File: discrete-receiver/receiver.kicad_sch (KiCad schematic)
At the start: 42 parts, among them J1 His Excellence, J3 Conn_01x04_Socket, J7 Her Excellency, T1 H1102NLT, T2 MABA-007159-000000, U16 PSA4-5043_, U18 SN74LVC1G3157DBVR, U19 SN74LVC1G3157DBVR, U2 OPA1612AxD, U20 SN74LVC1G3157DBVR, U3 OPA1612AxD, U5 ADE-12+

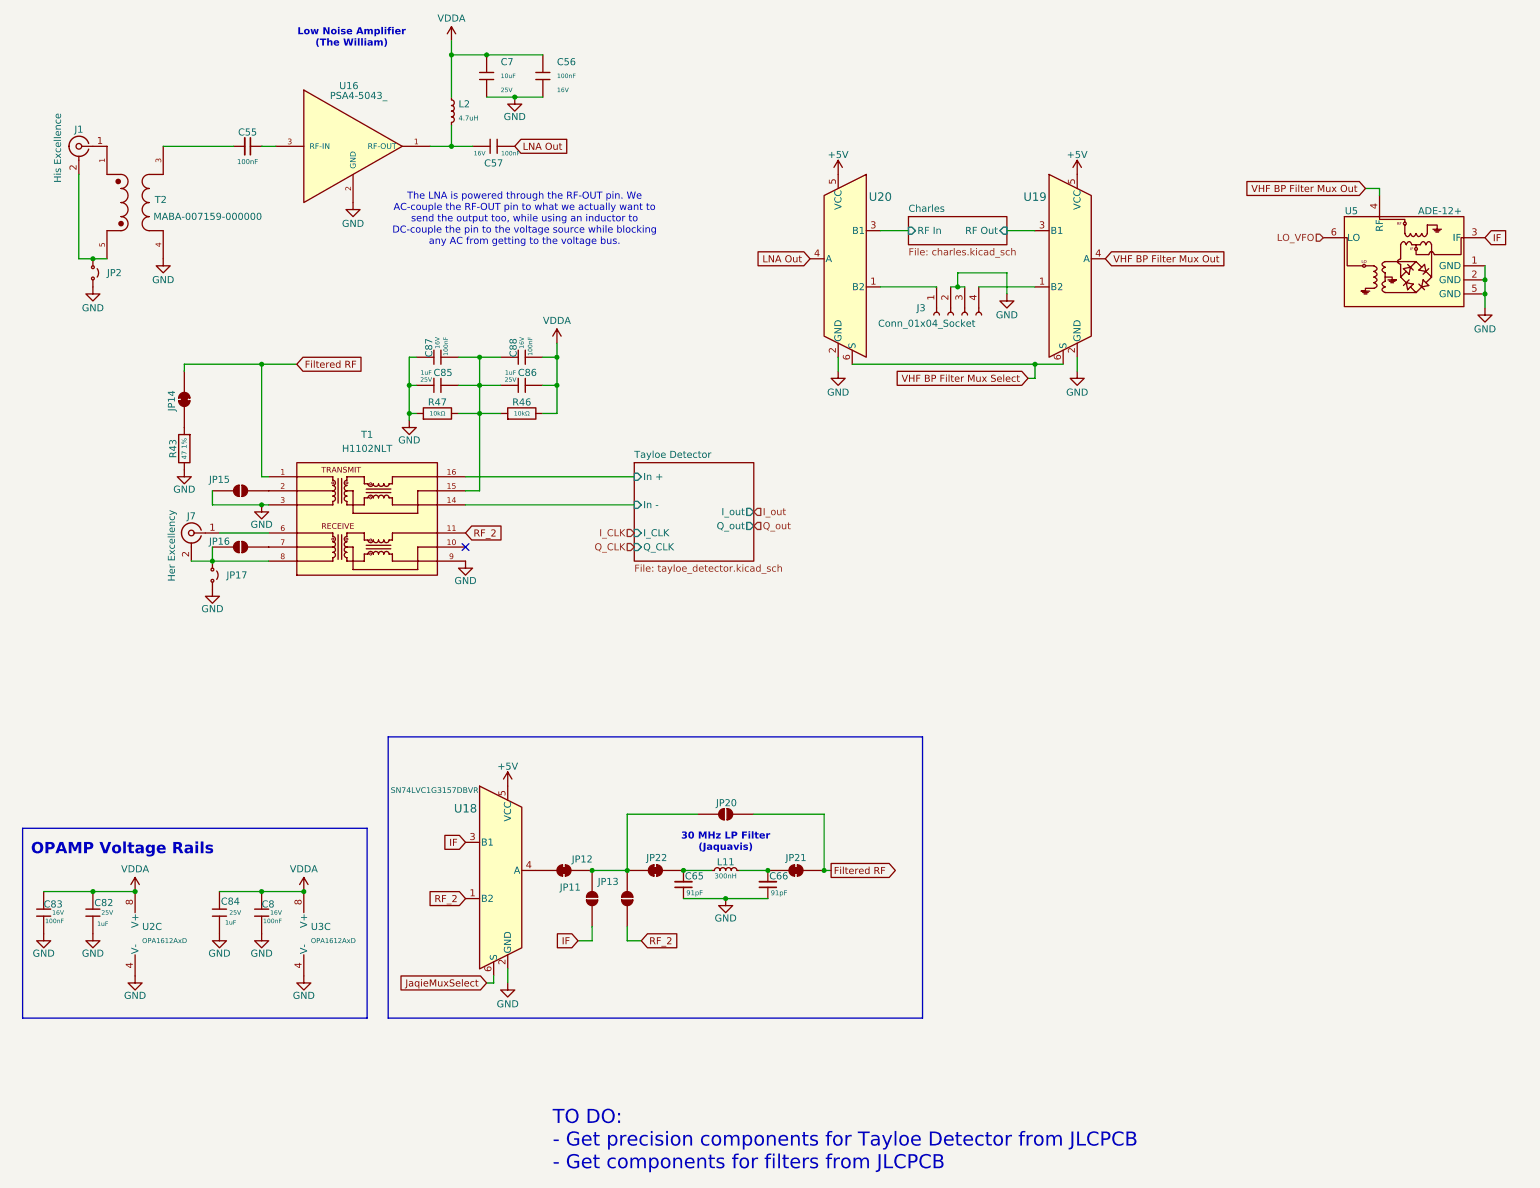
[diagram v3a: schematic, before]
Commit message: Subsheetified the receiver page
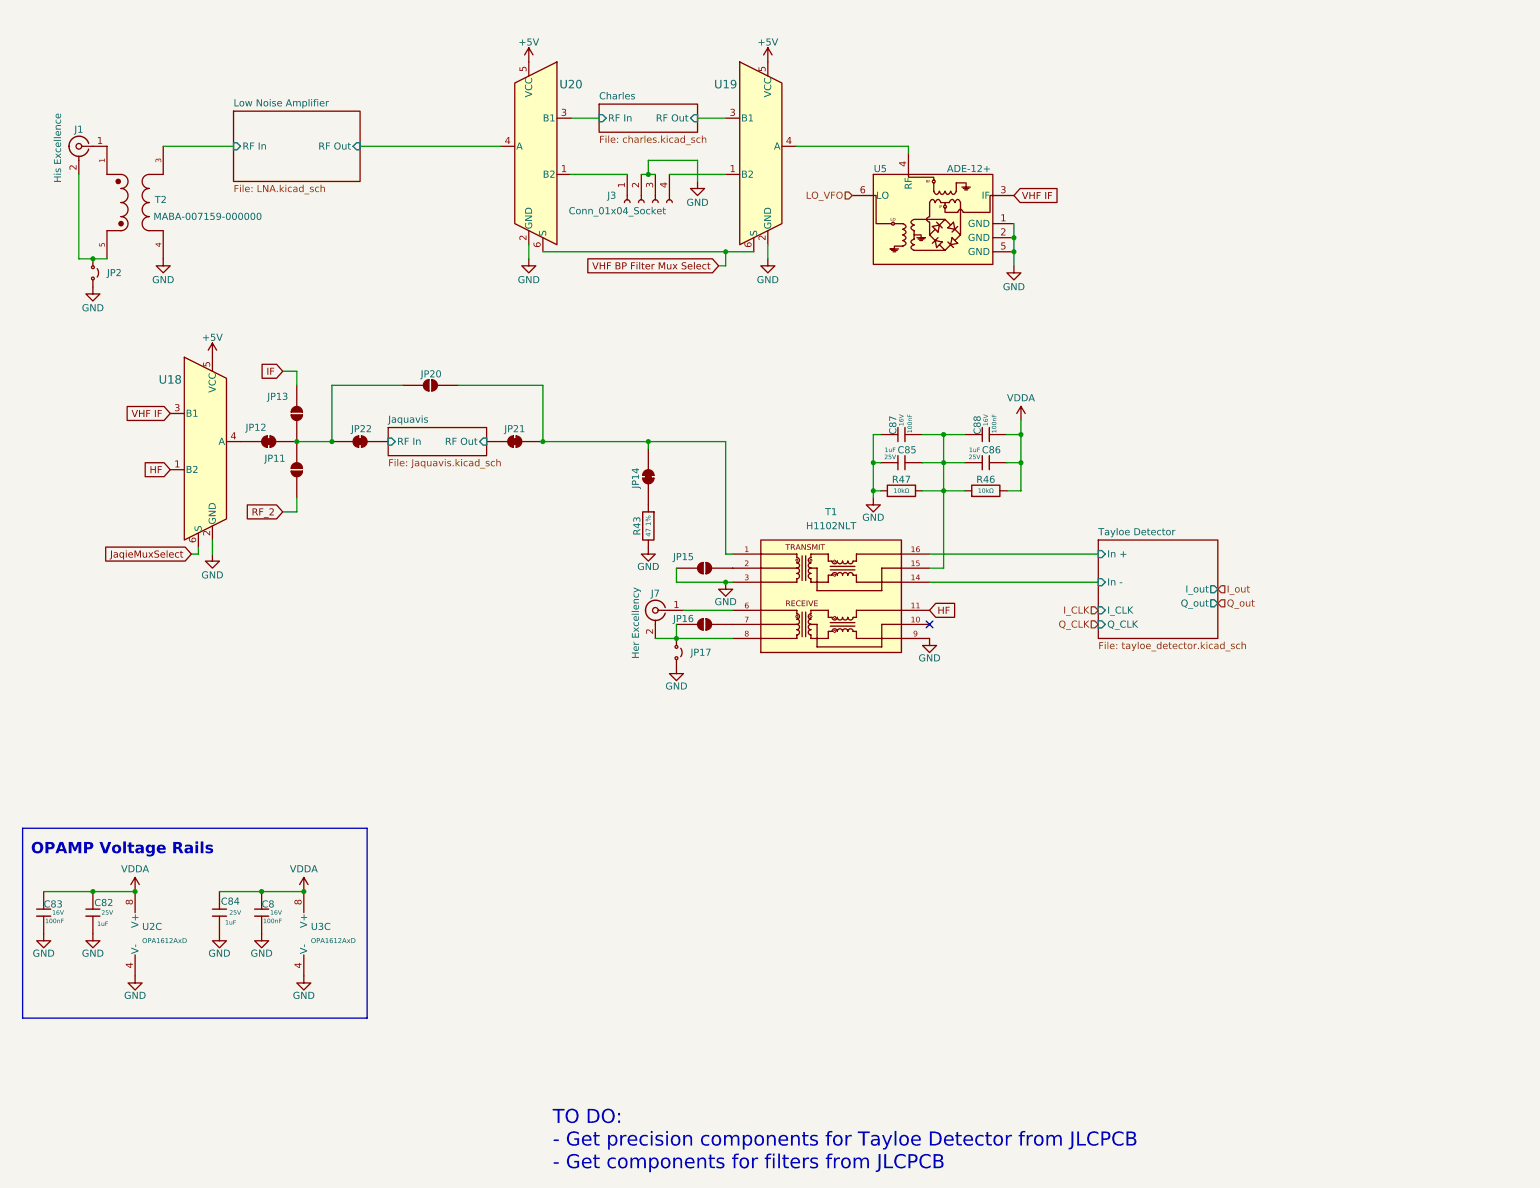
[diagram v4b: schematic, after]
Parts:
- removed C55: 100nF, symbol Device:C_Small
- removed C56, C57: 100nF, PCM_JLCPCB:C_0402, symbol PCM_JLCPCB-Capacitors:0402,100nF
- removed C65, C66: 91pF, symbol Device:C_Small
- removed C7: 10uF, PCM_JLCPCB:C_0603, symbol PCM_JLCPCB-Capacitors:0603,10uF,(2)
- removed L11: 300nH, symbol Device:L_Small
- removed L2: 4.7uH, symbol Device:L_Small
- removed U16: PSA4-5043_, PSA4-5043_:PSA4-5043_, symbol PSA4-5043_:PSA4-5043_
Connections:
- net IF: now also JP13.2 (B); no longer JP11.1 (A), U18.3 (B1), U5.3 (IF)
- net RF_2: now also JP11.1 (A); no longer JP13.1 (A), T1.11, U18.1 (B2)
- net at JP11.2 (B), JP12.2 (B), JP20.1 (A)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: now also JP13.1 (A); no longer JP13.2 (B)
- net Low Noise Amplifier/RF In: now reaches T2.3
- net Jaquavis/RF In: now reaches JP22.2 (B)
- net Jaquavis/RF Out: now reaches JP21.1 (A)
- net Filtered RF: no longer names the net of JP14.2 (B), JP20.2 (B), JP21.2 (B), T1.1
- net LNA Out renamed Low Noise Amplifier/RF Out
- net VHF BP Filter Mux Out: no longer names the net of U19.4 (A), U5.4 (RF)
- new net HF: T1.11, U18.1 (B2)
- new net VHF IF: U18.3 (B1), U5.3 (IF)
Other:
- added sheet Jaquavis (Jaquavis.kicad_sch)
- added sheet Low Noise Amplifier (LNA.kicad_sch)
- note removed: "30 MHz LP Filter (Jaquavis)"
- note removed: "Low Noise Amplifier (The William)"
- note removed: "The LNA is powered through the RF-OUT pin. We AC-couple the RF-OUT pin to what we actually want to send the output too, while using an inductor to DC-couple the pin to the voltage source while blocking any AC from getting to the voltage bus."
- moved on the sheet: C85, C86, C87, C88, J3, J7, JP14, JP15, JP16, JP17, R43, R46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

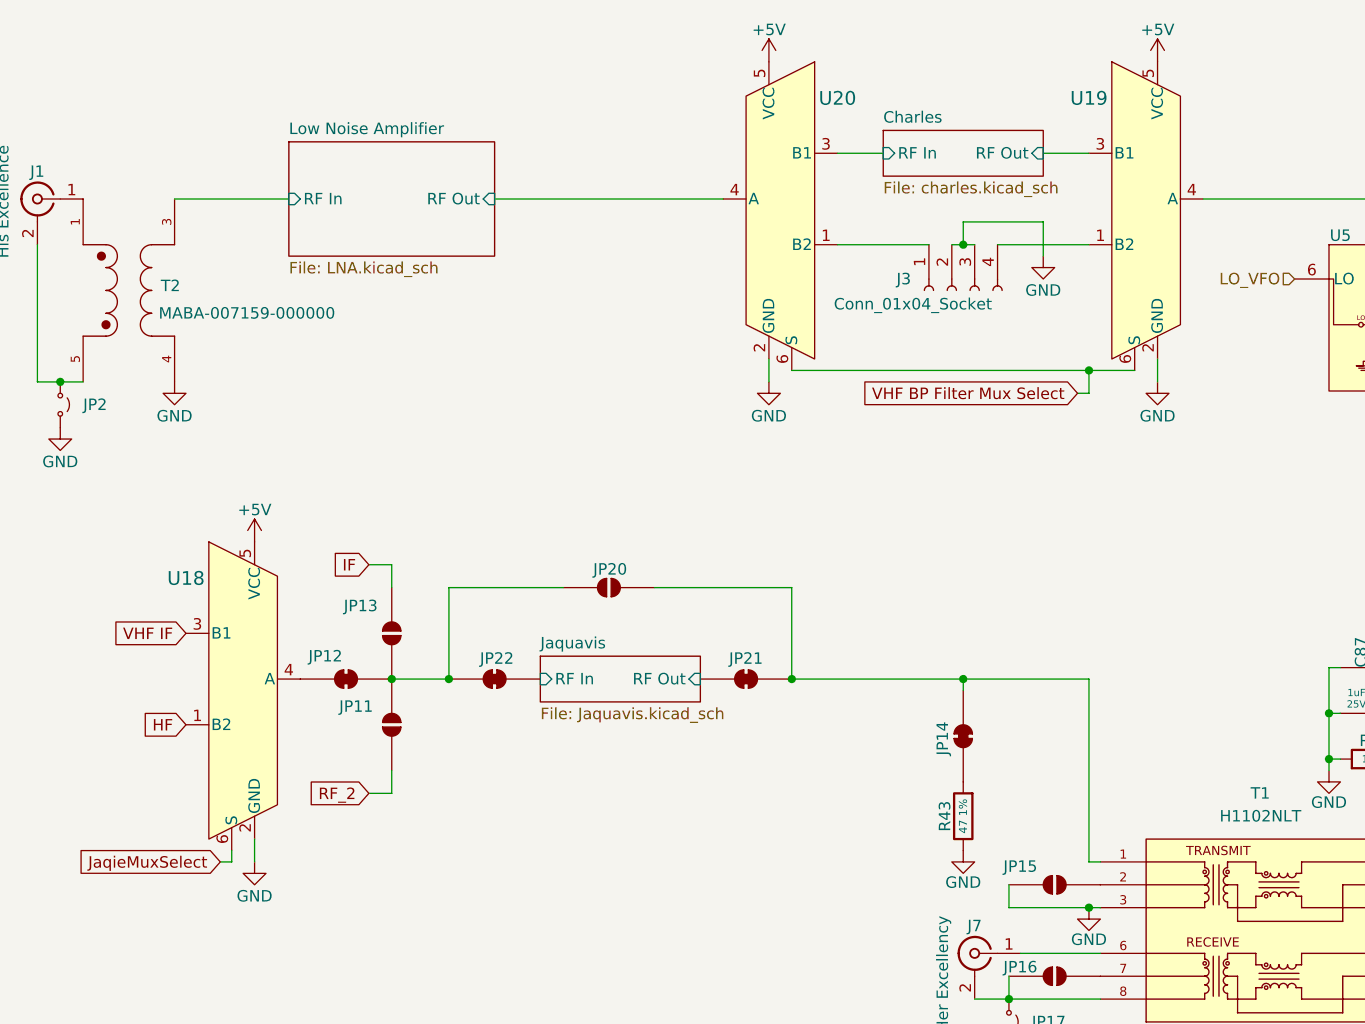
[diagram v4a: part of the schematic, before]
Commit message: Parts on receiver page have been JLC'd and given footprints
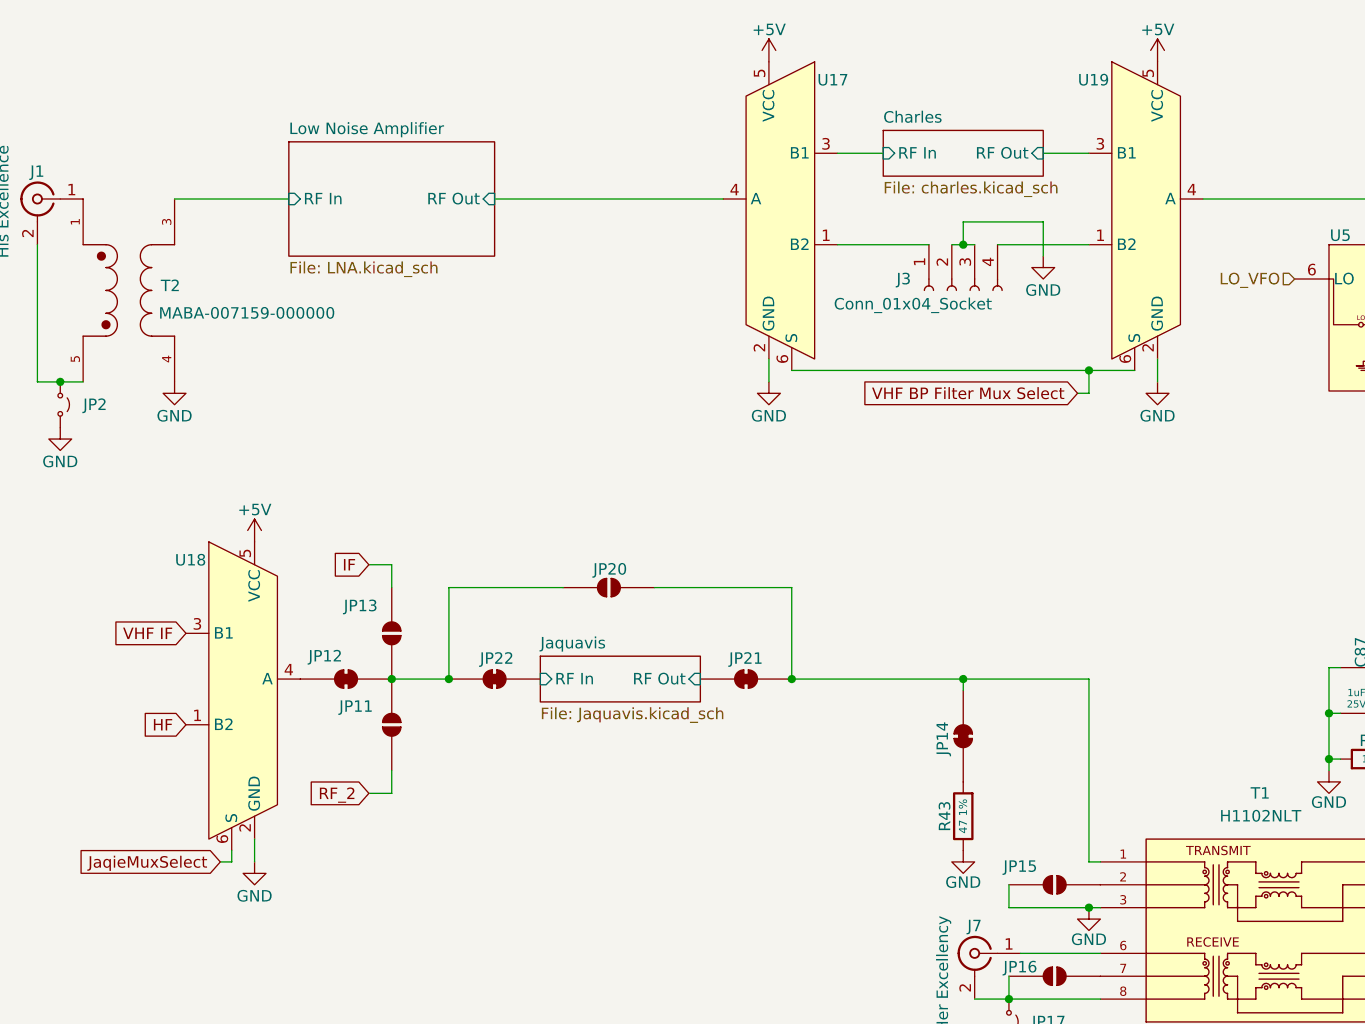
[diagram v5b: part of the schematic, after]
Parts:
- removed U18, U19, U20: SN74LVC1G3157DBVR, DBV6, symbol sdr_project:SN74LVC1G3157DBVR
- added U17, U18, U19: (no value), EasyEDA_Lib:SOT-23-6_L2.9-W1.6-P0.95-LS2.8-BR, symbol EasyEDA_Lib:SN74LVC1G3157DBVR
- R43: footprint (none) -> PCM_JLCPCB:R_0603; LCSC (none) -> C1002
- T1: LCSC (none) -> C20623173; MANUFACTURER Pulse Electronics -> (none); PARTREV NA -> (none); STNADARD Manufacturer Recommendation -> (none)
- U5: Height 2.08 -> (none); LCSC (none) -> C3176671; Manufacturer_Name Mini-Circuits -> (none); Manufacturer_Part_Number ADE-12+ -> (none); Mouser Part Number 139-ADE-12 -> (none); Mouser Price/Stock https://www.mouser.co.uk/ProductDetail/Mini-Circuits/ADE-12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 -> (none)
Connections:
- net +5V: now also U17.5 (VCC), U18.5 (VCC), U19.5 (VCC)
- net Charles/RF In: now also U17.3 (B1)
- net Charles/RF Out: now also U19.3 (B1)
- net GND: now also U17.2 (GND), U18.2 (GND), U19.2 (GND)
- net HF: now also U18.1 (B2)
- net JaqieMuxSelect: now also U18.6 (S)
- net Low Noise Amplifier/RF Out: now also U17.4 (A)
- net VHF BP Filter Mux Select: now also U17.6 (S), U19.6 (S)
- net VHF IF: now also U18.3 (B1)
- net at J3.1 (Pin_1): now also U17.1 (B2)
- net at J3.4 (Pin_4): now also U19.1 (B2)
- net at JP12.1 (A): now also U18.4 (A)
- net at U5.4 (RF): now also U19.4 (A)

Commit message: Progress made on schematic
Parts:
- removed C8, C83: 100nF, PCM_JLCPCB:C_0402, symbol PCM_JLCPCB-Capacitors:0402,100nF
- removed C82, C84: 1uF, PCM_JLCPCB:C_0402, symbol PCM_JLCPCB-Capacitors:0402,1uF
- removed U2: OPA1612AxD, Package_SO:SOIC-8_3.9x4.9mm_P1.27mm, symbol Amplifier_Operational:OPA1612AxD
- removed U3: OPA1612AxD, symbol Amplifier_Operational:OPA1612AxD
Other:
- note removed: "OPAMP Voltage Rails"

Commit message: Started to redo power
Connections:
- net VDDA renamed +5V_A

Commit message: AAAAH
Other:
- note added: "DC blocking cap"
- note added: "Recenter at 2.4V"
